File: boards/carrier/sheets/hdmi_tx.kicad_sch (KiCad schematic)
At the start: 14 parts, among them J1 HDMI-019S, U1 TPD12S016PWR, U2 24LC256T-I/SN

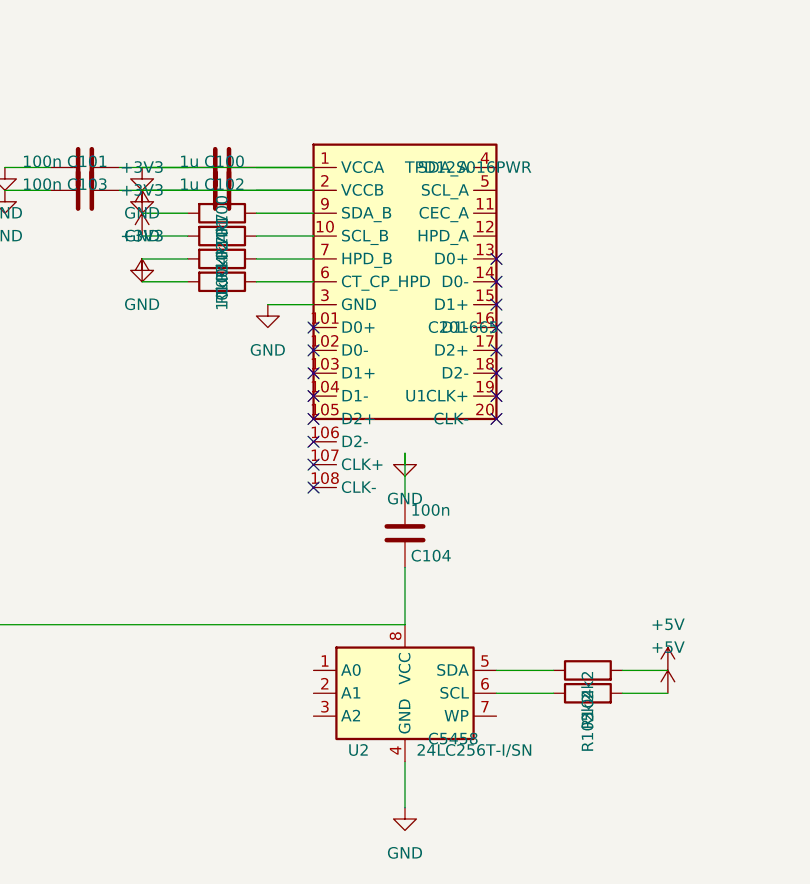
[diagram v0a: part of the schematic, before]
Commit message: place: auto-NC every IC pin not handled by overrides/cluster/power-paths
Default policy reversed: instead of NC'ing only pins explicitly listed
in the refcircuit's no_external_required, NC every IC pin we didn't
explicitly wire. A pin is "handled" if any of: pin_net_overrides /
net_overrides claim it, the cluster pass placed a passive against it,
it's the IC's primary supply pin (power_input_net / power_output_net
standard names), or it's a GND-family pin _attach_ic_ground covers.

Drops pin_not_connected ERC errors from ~45 → ~5 across the carrier
without requiring refcircuits to explicitly catalogue every unused pin
on every IC's symbol. A small visual cost (X mark on otherwise-bare
pins) for a clean baseline; refcircuits can still add explicit pin
handling when they want a nicer rendering.

  Before: 89 errors
  After:  44 errors
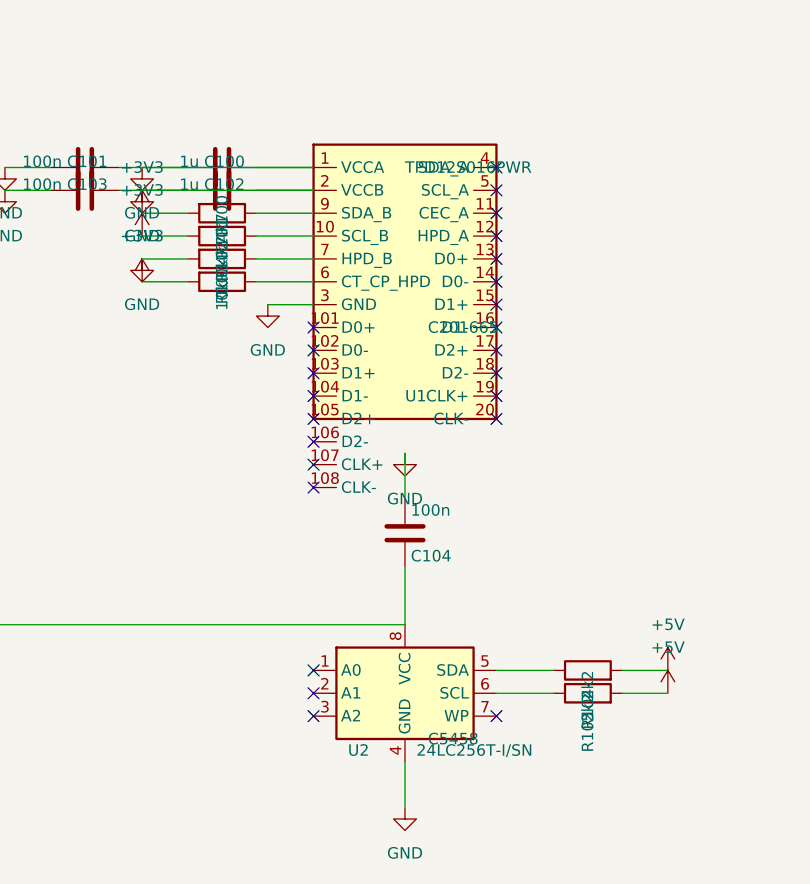
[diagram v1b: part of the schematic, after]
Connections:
- no-connect marks 16 -> 24
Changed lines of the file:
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@@
 		(instances
 			(project "HDMI Transmitter (Zynq → TPD12S016 → HDMI-A)"
-				(path "/c944d88d-9bf3-474f-aa95-e7aaccb28821"
+				(path "/b7e26b45-55d1-434b-bc9d-65189d73d5bd"
 					(reference "U1")
 					(unit 1)
@@
 		(instances
 			(project "HDMI Transmitter (Zynq → TPD12S016 → HDMI-A)"
-				(path "/c944d88d-9bf3-474f-aa95-e7aaccb28821"
+				(path "/b7e26b45-55d1-434b-bc9d-65189d73d5bd"
 					(reference "C100")
 					(unit 1)
@@
 		(instances
 			(project "HDMI Transmitter (Zynq → TPD12S016 → HDMI-A)"
-				(path "/c944d88d-9bf3-474f-aa95-e7aaccb28821"
+				(path "/b7e26b45-55d1-434b-bc9d-65189d73d5bd"
 					(reference "#PWR100")
 					(unit 1)
@@
 		(instances
 			(project "HDMI Transmitter (Zynq → TPD12S016 → HDMI-A)"
-				(path "/c944d88d-9bf3-474f-aa95-e7aaccb28821"
+				(path "/b7e26b45-55d1-434b-bc9d-65189d73d5bd"
 					(reference "C101")
 					(unit 1)
@@
 		(instances
 			(project "HDMI Transmitter (Zynq → TPD12S016 → HDMI-A)"
-				(path "/c944d88d-9bf3-474f-aa95-e7aaccb28821"
+				(path "/b7e26b45-55d1-434b-bc9d-65189d73d5bd"
 					(reference "#PWR101")
 					(unit 1)
@@
 		(instances
 			(project "HDMI Transmitter (Zynq → TPD12S016 → HDMI-A)"
-				(path "/c944d88d-9bf3-474f-aa95-e7aaccb28821"
+				(path "/b7e26b45-55d1-434b-bc9d-65189d73d5bd"
 					(reference "C102")
 					(unit 1)
@@
 		(instances
 			(project "HDMI Transmitter (Zynq → TPD12S016 → HDMI-A)"
-				(path "/c944d88d-9bf3-474f-aa95-e7aaccb28821"
+				(path "/b7e26b45-55d1-434b-bc9d-65189d73d5bd"
 					(reference "#PWR102")
 					(unit 1)
@@
 		(instances
 			(project "HDMI Transmitter (Zynq → TPD12S016 → HDMI-A)"
-				(path "/c944d88d-9bf3-474f-aa95-e7aaccb28821"
+				(path "/b7e26b45-55d1-434b-bc9d-65189d73d5bd"
 					(reference "C103")
 					(unit 1)
@@
 		(instances
 			(project "HDMI Transmitter (Zynq → TPD12S016 → HDMI-A)"
-				(path "/c944d88d-9bf3-474f-aa95-e7aaccb28821"
+				(path "/b7e26b45-55d1-434b-bc9d-65189d73d5bd"
 					(reference "#PWR103")
 					(unit 1)
@@
 		(instances
 			(project "HDMI Transmitter (Zynq → TPD12S016 → HDMI-A)"
-				(path "/c944d88d-9bf3-474f-aa95-e7aaccb28821"
+				(path "/b7e26b45-55d1-434b-bc9d-65189d73d5bd"
 					(reference "R100")
 					(unit 1)
@@
 		(instances
 			(project "HDMI Transmitter (Zynq → TPD12S016 → HDMI-A)"
-				(path "/c944d88d-9bf3-474f-aa95-e7aaccb28821"
+				(path "/b7e26b45-55d1-434b-bc9d-65189d73d5bd"
 					(reference "#PWR104")
 					(unit 1)
@@
 		(instances
 			(project "HDMI Transmitter (Zynq → TPD12S016 → HDMI-A)"
-				(path "/c944d88d-9bf3-474f-aa95-e7aaccb28821"
+				(path "/b7e26b45-55d1-434b-bc9d-65189d73d5bd"
 					(reference "R101")
 					(unit 1)
@@
 		(instances
 			(project "HDMI Transmitter (Zynq → TPD12S016 → HDMI-A)"
-				(path "/c944d88d-9bf3-474f-aa95-e7aaccb28821"
+				(path "/b7e26b45-55d1-434b-bc9d-65189d73d5bd"
 					(reference "#PWR105")
 					(unit 1)
@@
 		(instances
 			(project "HDMI Transmitter (Zynq → TPD12S016 → HDMI-A)"
-				(path "/c944d88d-9bf3-474f-aa95-e7aaccb28821"
+				(path "/b7e26b45-55d1-434b-bc9d-65189d73d5bd"
 					(reference "R102")
 					(unit 1)
@@
 		(instances
 			(project "HDMI Transmitter (Zynq → TPD12S016 → HDMI-A)"
-				(path "/c944d88d-9bf3-474f-aa95-e7aaccb28821"
+				(path "/b7e26b45-55d1-434b-bc9d-65189d73d5bd"
 					(reference "#PWR106")
 					(unit 1)
@@
 		(instances
 			(project "HDMI Transmitter (Zynq → TPD12S016 → HDMI-A)"
-				(path "/c944d88d-9bf3-474f-aa95-e7aaccb28821"
+				(path "/b7e26b45-55d1-434b-bc9d-65189d73d5bd"
 					(reference "R103")
 					(unit 1)
@@
 		(instances
 			(project "HDMI Transmitter (Zynq → TPD12S016 → HDMI-A)"
-				(path "/c944d88d-9bf3-474f-aa95-e7aaccb28821"
+				(path "/b7e26b45-55d1-434b-bc9d-65189d73d5bd"
 					(reference "#PWR107")
 					(unit 1)
@@
 		(instances
 			(project "HDMI Transmitter (Zynq → TPD12S016 → HDMI-A)"
-				(path "/c944d88d-9bf3-474f-aa95-e7aaccb28821"
+				(path "/b7e26b45-55d1-434b-bc9d-65189d73d5bd"
 					(reference "#PWR108")
 					(unit 1)
@@
 		(instances
 			(project "HDMI Transmitter (Zynq → TPD12S016 → HDMI-A)"
-				(path "/c944d88d-9bf3-474f-aa95-e7aaccb28821"
+				(path "/b7e26b45-55d1-434b-bc9d-65189d73d5bd"
 					(reference "U2")
 					(unit 1)
@@
 		(instances
 			(project "HDMI Transmitter (Zynq → TPD12S016 → HDMI-A)"
-				(path "/c944d88d-9bf3-474f-aa95-e7aaccb28821"
+				(path "/b7e26b45-55d1-434b-bc9d-65189d73d5bd"
 					(reference "C104")
 					(unit 1)
@@
 		(instances
 			(project "HDMI Transmitter (Zynq → TPD12S016 → HDMI-A)"
-				(path "/c944d88d-9bf3-474f-aa95-e7aaccb28821"
+				(path "/b7e26b45-55d1-434b-bc9d-65189d73d5bd"
 					(reference "#PWR109")
 					(unit 1)
@@
 		(instances
 			(project "HDMI Transmitter (Zynq → TPD12S016 → HDMI-A)"
-				(path "/c944d88d-9bf3-474f-aa95-e7aaccb28821"
+				(path "/b7e26b45-55d1-434b-bc9d-65189d73d5bd"
 					(reference "R104")
 					(unit 1)
@@
 		(instances
 			(project "HDMI Transmitter (Zynq → TPD12S016 → HDMI-A)"
-				(path "/c944d88d-9bf3-474f-aa95-e7aaccb28821"
+				(path "/b7e26b45-55d1-434b-bc9d-65189d73d5bd"
 					(reference "#PWR110")
 					(unit 1)
@@
 		(instances
 			(project "HDMI Transmitter (Zynq → TPD12S016 → HDMI-A)"
-				(path "/c944d88d-9bf3-474f-aa95-e7aaccb28821"
+				(path "/b7e26b45-55d1-434b-bc9d-65189d73d5bd"
 					(reference "R105")
 					(unit 1)
@@
 		(instances
 			(project "HDMI Transmitter (Zynq → TPD12S016 → HDMI-A)"
-				(path "/c944d88d-9bf3-474f-aa95-e7aaccb28821"
+				(path "/b7e26b45-55d1-434b-bc9d-65189d73d5bd"
 					(reference "#PWR111")
 					(unit 1)
@@
 		(instances
 			(project "HDMI Transmitter (Zynq → TPD12S016 → HDMI-A)"
-				(path "/c944d88d-9bf3-474f-aa95-e7aaccb28821"
+				(path "/b7e26b45-55d1-434b-bc9d-65189d73d5bd"
 					(reference "#PWR112")
 					(unit 1)
@@
 		(instances
 			(project "HDMI Transmitter (Zynq → TPD12S016 → HDMI-A)"
-				(path "/c944d88d-9bf3-474f-aa95-e7aaccb28821"
+				(path "/b7e26b45-55d1-434b-bc9d-65189d73d5bd"
 					(reference "J1")
 					(unit 1)
@@
 		(instances
 			(project "HDMI Transmitter (Zynq → TPD12S016 → HDMI-A)"
-				(path "/c944d88d-9bf3-474f-aa95-e7aaccb28821"
+				(path "/b7e26b45-55d1-434b-bc9d-65189d73d5bd"
 					(reference "#PWR113")
 					(unit 1)
@@
 	)
 	(no_connect
+		(at 139.7 46.99)
+	)
+	(no_connect
+		(at 139.7 49.53)
+	)
+	(no_connect
+		(at 139.7 52.07)
+	)
+	(no_connect
+		(at 139.7 54.61)
+	)
+	(no_connect
 		(at 139.7 57.15)
 	)
@@
 		(at 139.7 74.93)
 	)
+	(no_connect
+		(at 119.38 102.87)
+	)
+	(no_connect
+		(at 119.38 105.41)
+	)
+	(no_connect
+		(at 119.38 107.95)
+	)
+	(no_connect
+		(at 139.7 107.95)
+	)
 	(sheet_instances
